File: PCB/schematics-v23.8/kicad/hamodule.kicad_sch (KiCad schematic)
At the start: 140 parts, among them J1 GND|5V, J10 Tx|Rx, J11 USB_C_Receptacle_USB2.0, J12 2604-1104, J14 2604-1104, J15 2604-1104, J2 2604-1102, J3 Sda|Scl, J4 13|12, J5 9|3|16, J6 GND|3.3V, J7 Conn_01x02_Pin, J9 2604-1104, K1 AQG12205, K2 AQG12205, K3 AQG12205, K4 AQG12205, K5 AQG12205, K6 AQG12205, K7 AQG12205, K8 AQG12205, SW1 Reset, SW2 Boot, SW3 USB | PS, U1 LD1117AV33, U10 ULN2803A, U2 ESP32-S3-WROOM-2, U3 LDA210-PDIP, U4 USBLC6-2SC6, U5 LDA210-PDIP, U6 LDA210-PDIP, U7 SHT4x, U8 LDA210-PDIP, U9 MCP23017_SO

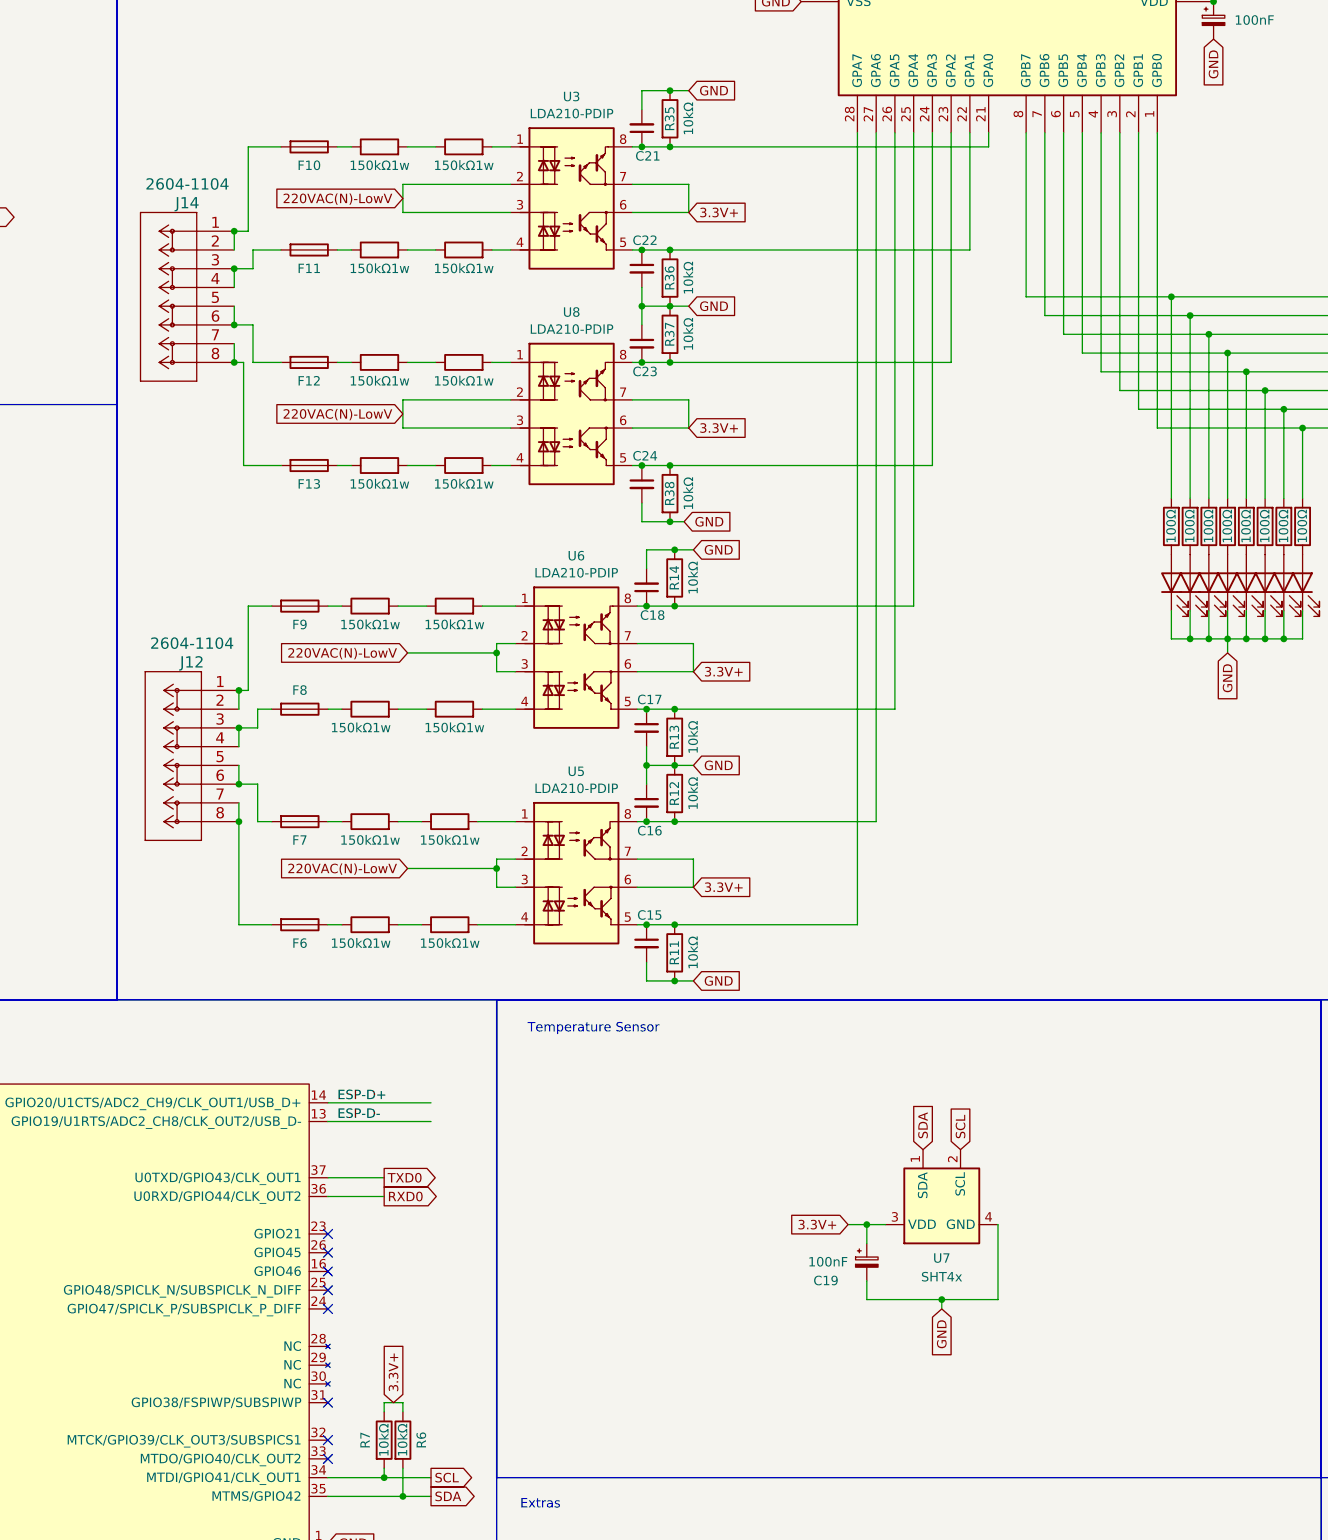
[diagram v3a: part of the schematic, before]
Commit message: [V23.8] Adding screen connector + Fixing version + adding caps
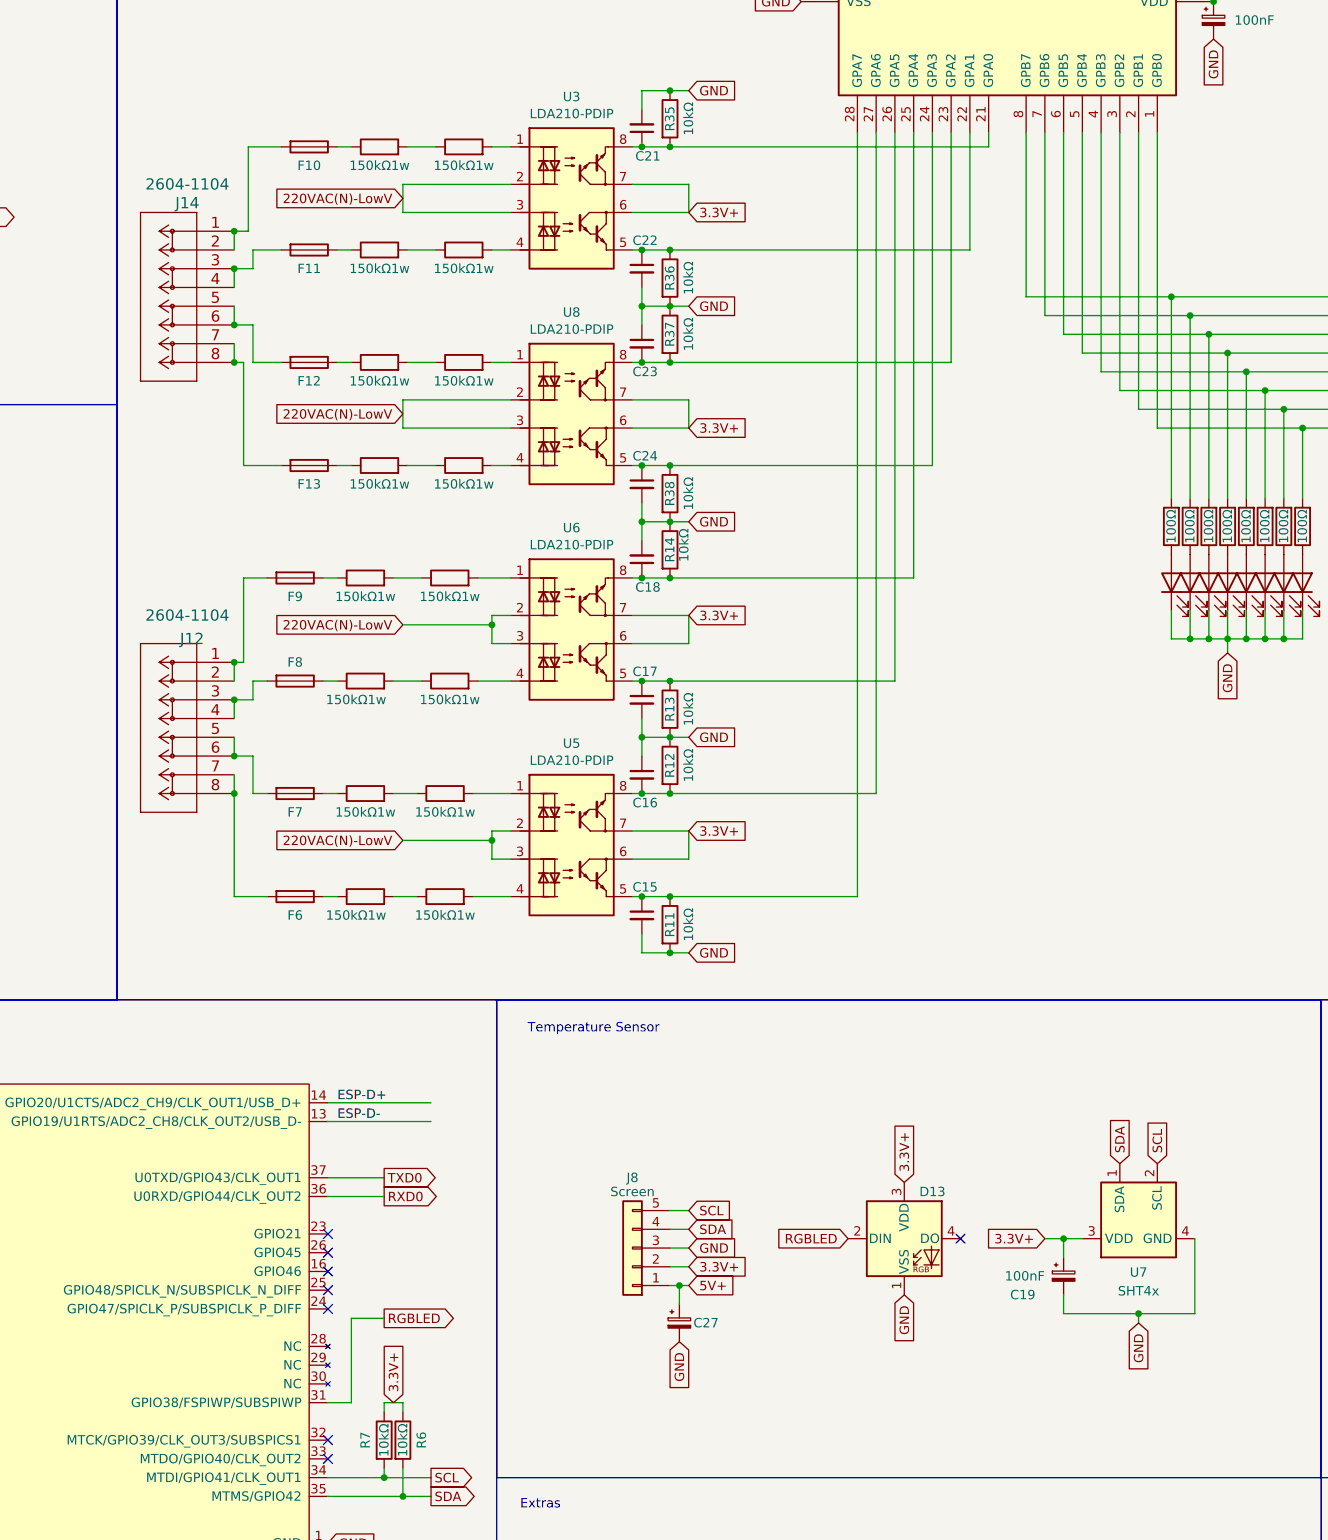
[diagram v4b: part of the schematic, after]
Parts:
- added C27: 22uF, Capacitor_SMD:C_0805_2012Metric_Pad1.18x1.45mm_HandSolder, symbol Device:C_Polarized_Small
- added D13: Inolux_IN-PI554FCH, LED_SMD:LED_Inolux_IN-PI554FCH_PLCC4_5.0x5.0mm_P3.2mm, symbol LED:Inolux_IN-PI554FCH
- added J8: Screen, Connector_JST:JST_XH_B5B-XH-A_1x05_P2.50mm_Vertical, symbol Connector_Generic:Conn_01x05
- C14: footprint Capacitor_SMD:C_0603_1608Metric_Pad1.08x0.95mm_HandSolder -> Capacitor_SMD:C_0805_2012Metric_Pad1.18x1.45mm_HandSolder
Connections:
- net 3.3V+: now also D13.3 (VDD), J8.2 (Pin_2)
- net 5V+: now also C27.1, J8.1 (Pin_1)
- net GND: now also C27.2, D13.1 (VSS), J8.3 (Pin_3)
- net SCL: now also J8.5 (Pin_5)
- net SDA: now also J8.4 (Pin_4)
- net RGBLED: now reaches U2.31 (GPIO38/FSPIWP/SUBSPIWP)
- net RGBLED: now also D13.2 (DIN)
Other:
- moved on the sheet: C15, C16, C17, C18, C19, F6, F7, F8, F9, J12, R11, R12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

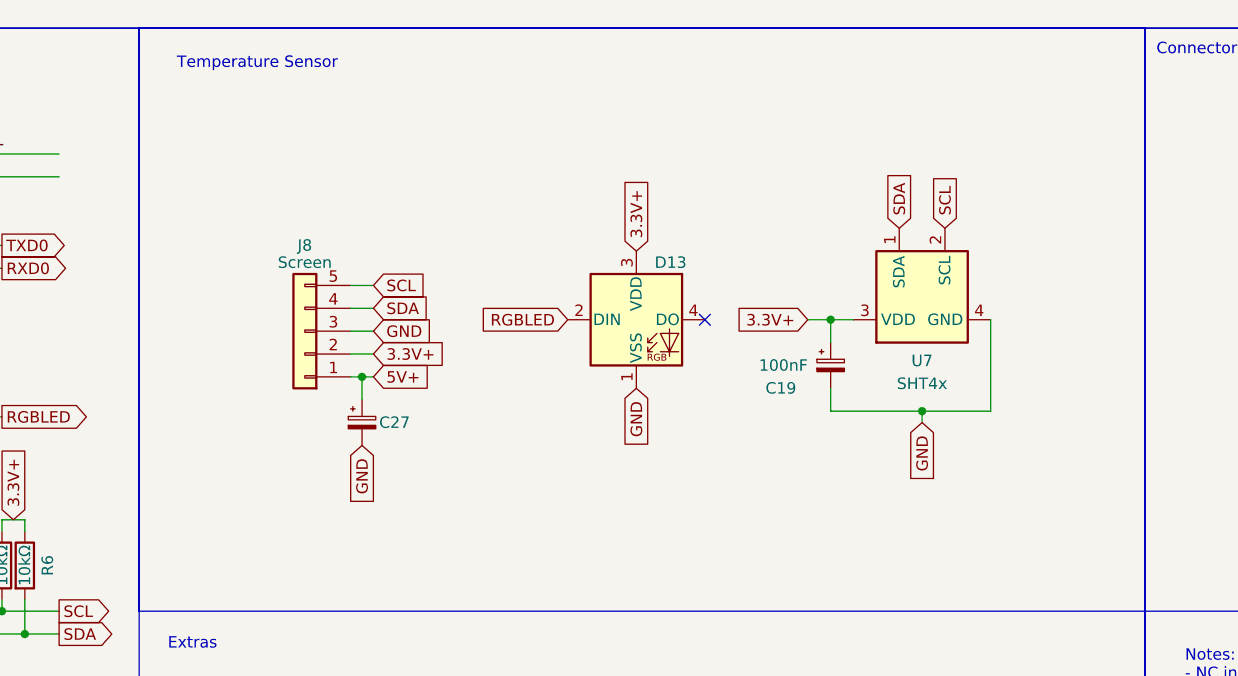
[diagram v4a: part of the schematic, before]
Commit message: adding RGB Led
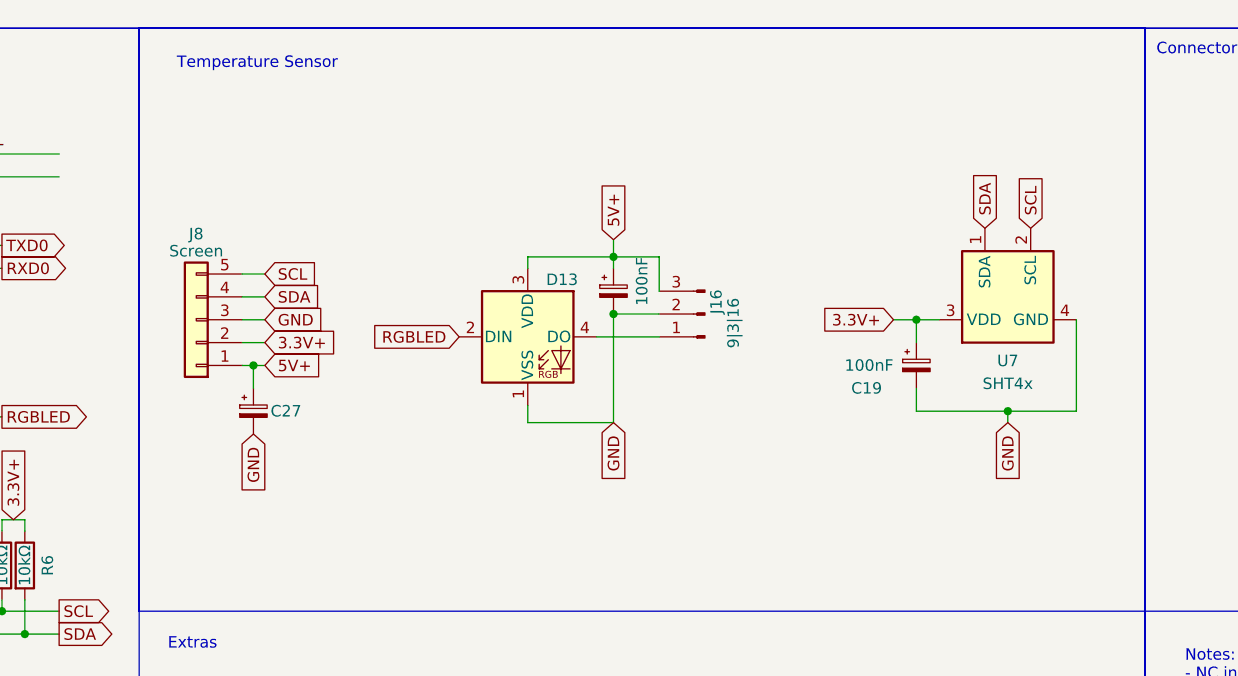
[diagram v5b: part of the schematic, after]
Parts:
- added C28: 100nF, Capacitor_SMD:C_0603_1608Metric_Pad1.08x0.95mm_HandSolder, symbol Device:C_Polarized_Small
- added J16: 9|3|16, Connector_PinHeader_2.54mm:PinHeader_1x03_P2.54mm_Vertical, symbol Connector:Conn_01x03_Pin
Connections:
- net 3.3V+: no longer D13.3 (VDD)
- net 5V+: now also D13.3 (VDD), C28.1, J16.3 (Pin_3)
- net GND: now also C28.2, J16.2 (Pin_2)
- net at D13.4 (DO): now also J16.1 (Pin_1)
- no-connect marks 27 -> 26
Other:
- moved on the sheet: C19, C27, D13, J8, U7

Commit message: [23.8] Adding RGB Led, fixing placing and silkscreen
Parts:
- added C29, C30: 100nF, Capacitor_SMD:C_0805_2012Metric_Pad1.18x1.45mm_HandSolder, symbol Device:C_Polarized_Small
- added R45: 10kΩ, Resistor_SMD:R_0603_1608Metric_Pad0.98x0.95mm_HandSolder, symbol Device:R
- added U12: SN74LV1T34DBV, Package_TO_SOT_SMD:SOT-23-5, symbol Logic_LevelTranslator:SN74LV1T34DBV
- C27: value 22uF -> 100nF
- J16: value 9|3|16 -> 5v|GND|Do
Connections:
- net 3.3V+: now also C29.1, C30.1; no longer C25.1
- net 5V+: now also C25.1, U12.5 (VCC)
- net GND: now also C29.2, C30.2, R45.1, U12.3 (GND)
- net RGBLED: now also R45.2, U12.2 (A); no longer D13.2 (DIN)
- new net: D13.2 (DIN), U12.4 (Y)
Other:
- moved on the sheet: C19, C27, D13, J16, J8, U7

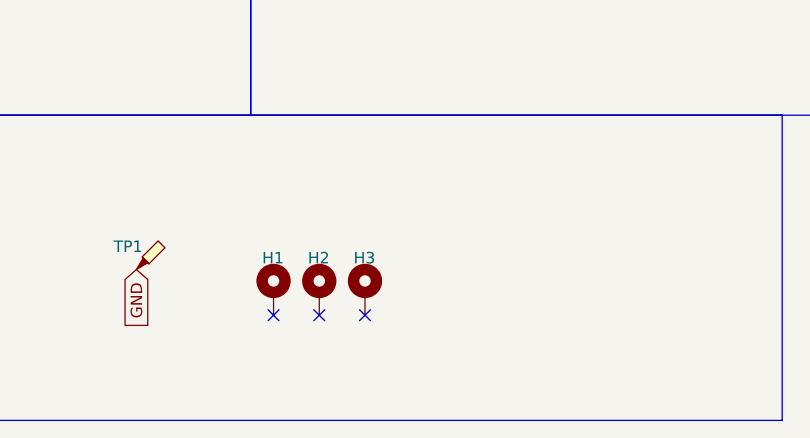
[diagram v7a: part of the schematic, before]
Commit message: reducing board size
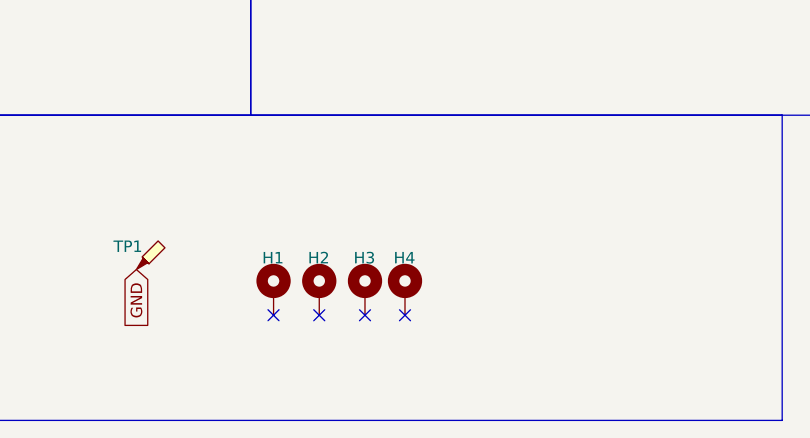
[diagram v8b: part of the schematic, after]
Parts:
- added H4: MountingHole_Pad, MountingHole:MountingHole_3.2mm_M3_ISO14580_Pad, symbol Mechanical:MountingHole_Pad
- C4: footprint Capacitor_SMD:C_0603_1608Metric_Pad1.08x0.95mm_HandSolder -> Capacitor_SMD:C_0805_2012Metric_Pad1.18x1.45mm_HandSolder
- C9: footprint Capacitor_SMD:C_0603_1608Metric_Pad1.08x0.95mm_HandSolder -> Capacitor_SMD:C_0805_2012Metric_Pad1.18x1.45mm_HandSolder; JLCPCB C14663 -> (none); LCSC C14663 -> (none)
- R8: footprint Resistor_SMD:R_2512_6332Metric_Pad1.40x3.35mm_HandSolder -> Resistor_SMD:R_0805_2012Metric_Pad1.20x1.40mm_HandSolder; JLCPCB C25719 -> (none); LCSC C25719 -> (none)
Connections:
- no-connect marks 26 -> 27
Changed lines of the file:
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@@
   (no_connect (at 45.085 240.665))
   (no_connect (at 45.085 215.265))
+  (no_connect (at 255.905 271.78))
   (no_connect (at 45.085 220.345))
   (no_connect (at 241.3 271.78))
@@
       (effects (font (size 1.27 1.27)) (justify right))
     )
-    (property "Footprint" "Capacitor_SMD:C_0603_1608Metric_Pad1.08x0.95mm_HandSolder" (at 83.5152 90.17 0)
+    (property "Footprint" "Capacitor_SMD:C_0805_2012Metric_Pad1.18x1.45mm_HandSolder" (at 83.5152 90.17 0)
       (effects (font (size 1.27 1.27)) hide)
     )
@@
       (effects (font (size 1.27 1.27)) hide)
     )
-    (property "JLCPCB" "C14663" (at 82.55 86.36 0)
+    (property "JLCPCB" "" (at 82.55 86.36 0)
       (effects (font (size 1.27 1.27)) hide)
     )
-    (property "LCSC" "C14663" (at 82.55 86.36 0)
+    (property "LCSC" "" (at 82.55 86.36 0)
       (effects (font (size 1.27 1.27)) hide)
     )
+    (property "PcbText" "" (at 82.55 86.36 0)
+      (effects (font (size 1.27 1.27)))
+    )
     (pin "1")
     (pin "2")
@@
       (effects (font (size 1.27 1.27)) (justify right))
     )
-    (property "Footprint" "Capacitor_SMD:C_0603_1608Metric_Pad1.08x0.95mm_HandSolder" (at 46.6852 90.17 0)
+    (property "Footprint" "Capacitor_SMD:C_0805_2012Metric_Pad1.18x1.45mm_HandSolder" (at 46.6852 90.17 0)
       (effects (font (size 1.27 1.27)) hide)
     )
@@
       (effects (font (size 1.27 1.27)) hide)
     )
+    (property "PcbText" "" (at 45.72 86.36 0)
+      (effects (font (size 1.27 1.27)))
+    )
     (pin "1")
     (pin "2")
@@
       (effects (font (size 1.27 1.27)))
     )
-    (property "Footprint" "Resistor_SMD:R_2512_6332Metric_Pad1.40x3.35mm_HandSolder" (at 41.275 158.623 90)
+    (property "Footprint" "Resistor_SMD:R_0805_2012Metric_Pad1.20x1.40mm_HandSolder" (at 41.275 158.623 90)
       (effects (font (size 1.27 1.27)) hide)
     )
@@
       (effects (font (size 1.27 1.27)) hide)
     )
-    (property "JLCPCB" "C25719" (at 41.275 156.845 0)
+    (property "JLCPCB" "" (at 41.275 156.845 0)
       (effects (font (size 1.27 1.27)) hide)
     )
-    (property "LCSC" "C25719" (at 41.275 156.845 0)
+    (property "LCSC" "" (at 41.275 156.845 0)
       (effects (font (size 1.27 1.27)) hide)
     )
+    (property "PcbText" "" (at 41.275 156.845 0)
+      (effects (font (size 1.27 1.27)))
+    )
     (pin "1")
     (pin "2")
@@
         )
       )
+    )
+  )
+  (symbol (lib_id "Mechanical:MountingHole_Pad") (at 255.905 269.24 0) (unit 1)
+    (in_bom yes) (on_board yes) (dnp no)
+    (property "Reference" "H4" (at 254.635 265.43 0)
+      (effects (font (size 1.27 1.27)) (justify left))
+    )
+    (property "Value" "MountingHole_Pad" (at 258.445 270.3068 0)
+      (effects (font (size 1.27 1.27)) (justify left) hide)
+    )
+    (property "Footprint" "MountingHole:MountingHole_3.2mm_M3_ISO14580_Pad" (at 255.905 269.24 0)
+      (effects (font (size 1.27 1.27)) hide)
+    )
+    (property "Datasheet" "~" (at 255.905 269.24 0)
+      (effects (font (size 1.27 1.27)) hide)
+    )
+    (pin "1")
+    (instances
+      (project "hamodule"
+        (path "/e5217a0c-7f55-4c30-adda-7f8d95709d1b"
+          (reference "H4") (unit 1)
+        )
+      )
